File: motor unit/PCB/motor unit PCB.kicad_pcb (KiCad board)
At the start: 2 copper layers, 17.5 x 17.1 mm, 6 parts, among them M1 2RB18Z1B5, P1 CONN, Q1 2N7002

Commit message: Update motor unit PCB files
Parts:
- moved D1 8.71 mm to (161.5, 75.9)
- moved P1 8.13 mm to (159.0, 64.5), turned to 90 degrees
- moved C1 5.06 mm to (168.7, 64.3), turned to 180 degrees
- moved M1 4.26 mm to (168.7, 67.8)
- moved Q1 3.42 mm to (161.5, 72.4)
- moved R1 2.60 mm to (161.5, 68.3)
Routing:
- net Net-(C1-Pad2): track 30.5 -> 17.5 mm
- net +5V: track 14.9 -> 3.77 mm
- net GND: track 4.50 -> 7.86 mm
- net Net-(P1-Pad3): track 9.94 -> 7.86 mm
- added copper zone on F.Cu, net +5V
- removed copper zone on F.Cu, net GND

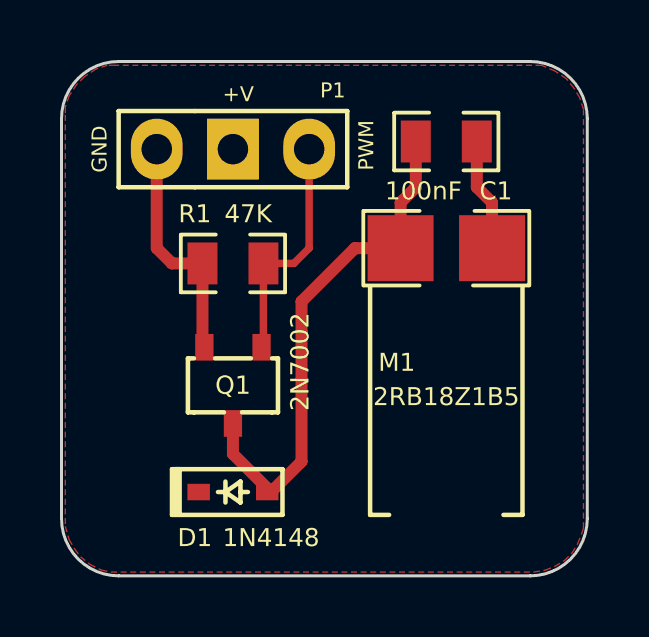
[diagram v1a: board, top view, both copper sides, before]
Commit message: Update motor unit 3D and PCB
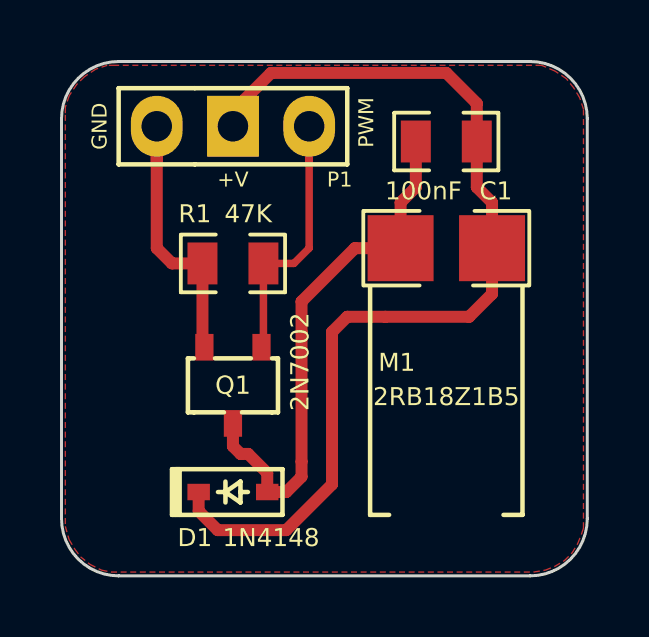
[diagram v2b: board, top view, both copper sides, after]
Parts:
- moved P1 0.76 mm to (159.0, 63.8)
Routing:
- net +5V: track 3.77 -> 33.1 mm
- net Net-(P1-Pad3): track 7.86 -> 9.13 mm
- net GND: track 7.86 -> 9.13 mm
- net Net-(C1-Pad2): track 17.5 -> 18.0 mm
- added copper zone on F.Cu, net GND
- removed copper zone on F.Cu, net +5V
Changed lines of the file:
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@@
     (links 10)
     (no_connects 0)
-    (area 155.778999 61.544999 173.405001 78.790001)
+    (area 153.557572 61.544999 173.405001 78.790001)
     (thickness 1.6)
     (drawings 8)
-    (tracks 25)
+    (tracks 48)
     (zones 0)
     (modules 6)
@@
   )
   (module Pin_Header_Straight_1x03_MOD (layer F.Cu)
-    (at 159.004 64.516 90)
+    (at 159.004 63.754 90)
     (descr "Through hole pin header")
     (tags "pin header")
-    (fp_text reference P1 (at 1.9558 5.8674 180) (layer F.SilkS)
+    (fp_text reference P1 (at -1.778 6.096 180) (layer F.SilkS)
       (effects (font (size 0.5 0.5) (thickness 0.125)))
     )
@@
       (effects (font (size 0.5 0.5) (thickness 0.125)))
     )
-    (fp_text user +V (at 1.8288 2.7178 180) (layer F.SilkS)
+    (fp_text user +V (at -1.778 2.54 180) (layer F.SilkS)
       (effects (font (size 0.5 0.5) (thickness 0.125)))
     )
@@
   (gr_arc (start 157.734 63.5) (end 155.829 63.5) (angle 90) (layer Edge.Cuts) (width 0.1))
   (gr_arc (start 171.45 63.5) (end 171.45 61.595) (angle 90) (layer Edge.Cuts) (width 0.1))
+  (segment (start 162.687 75.946) (end 163.322 75.946) (width 0.4) (layer F.Cu) (net 1))
   (segment (start 163.83 70.612) (end 163.83 69.596) (width 0.4) (layer F.Cu) (net 1))
   (segment (start 163.83 74.93) (end 163.83 70.612) (width 0.4) (layer F.Cu) (net 1))
-  (segment (start 162.814 75.946) (end 163.83 74.93) (width 0.4) (layer F.Cu) (net 1))
   (segment (start 165.608 67.818) (end 167.132 67.818) (width 0.4) (layer F.Cu) (net 1))
   (segment (start 163.83 69.596) (end 165.608 67.818) (width 0.4) (layer F.Cu) (net 1))
+  (segment (start 163.83 75.438) (end 163.83 74.93) (width 0.4) (layer F.Cu) (net 1))
+  (segment (start 163.322 75.946) (end 163.83 75.438) (width 0.4) (layer F.Cu) (net 1))
+  (segment (start 162.687 75.946) (end 162.687 75.311) (width 0.4) (layer F.Cu) (net 1))
+  (segment (start 161.544 74.422) (end 161.544 73.66) (width 0.4) (layer F.Cu) (net 1))
+  (segment (start 161.798 74.676) (end 161.544 74.422) (width 0.4) (layer F.Cu) (net 1))
+  (segment (start 162.052 74.676) (end 161.798 74.676) (width 0.4) (layer F.Cu) (net 1))
+  (segment (start 162.687 75.311) (end 162.052 74.676) (width 0.4) (layer F.Cu) (net 1))
+  (segment (start 162.687 75.946) (end 162.814 75.946) (width 0.4) (layer F.Cu) (net 1))
+  (segment (start 167.132 66.294) (end 167.132 67.818) (width 0.4) (layer F.Cu) (net 1))
   (segment (start 167.64 64.262) (end 167.64 65.786) (width 0.4) (layer F.Cu) (net 1))
   (segment (start 167.64 65.786) (end 167.132 66.294) (width 0.4) (layer F.Cu) (net 1))
-  (segment (start 167.132 66.294) (end 167.132 67.818) (width 0.4) (layer F.Cu) (net 1))
-  (segment (start 162.687 75.946) (end 162.814 75.946) (width 0.4) (layer F.Cu) (net 1))
-  (segment (start 161.544 73.66) (end 161.544 74.676) (width 0.4) (layer F.Cu) (net 1))
-  (segment (start 161.544 74.676) (end 162.687 75.819) (width 0.4) (layer F.Cu) (net 1))
-  (segment (start 162.687 75.819) (end 162.687 75.946) (width 0.4) (layer F.Cu) (net 1))
+  (segment (start 159.004 63.754) (end 159.004 65.024) (width 0.4) (layer F.Cu) (net 2) (status 400000))
+  (segment (start 159.004 67.818) (end 159.512 68.326) (width 0.4) (layer F.Cu) (net 2))
+  (segment (start 159.512 68.326) (end 160.528 68.326) (width 0.4) (layer F.Cu) (net 2))
+  (segment (start 159.004 64.516) (end 159.004 65.024) (width 0.4) (layer F.Cu) (net 2))
+  (segment (start 159.004 65.024) (end 159.004 67.818) (width 0.4) (layer F.Cu) (net 2))
+  (segment (start 160.528 71.0565) (end 160.5915 71.12) (width 0.4) (layer F.Cu) (net 2))
   (segment (start 160.528 68.326) (end 160.528 71.0565) (width 0.4) (layer F.Cu) (net 2))
-  (segment (start 160.528 71.0565) (end 160.5915 71.12) (width 0.4) (layer F.Cu) (net 2))
-  (segment (start 159.004 64.516) (end 159.004 67.818) (width 0.4) (layer F.Cu) (net 2))
-  (segment (start 159.512 68.326) (end 160.528 68.326) (width 0.4) (layer F.Cu) (net 2))
-  (segment (start 159.004 67.818) (end 159.512 68.326) (width 0.4) (layer F.Cu) (net 2))
+  (segment (start 161.544 63.754) (end 161.544 63.246) (width 0.4) (layer F.Cu) (net 3) (status C00000))
+  (segment (start 161.544 63.246) (end 162.814 61.976) (width 0.4) (layer F.Cu) (net 3) (status 400000))
+  (segment (start 162.814 61.976) (end 168.656 61.976) (width 0.4) (layer F.Cu) (net 3))
+  (segment (start 168.656 61.976) (end 169.672 62.992) (width 0.4) (layer F.Cu) (net 3))
+  (segment (start 169.672 62.992) (end 169.672 64.262) (width 0.4) (layer F.Cu) (net 3) (status 800000))
+  (segment (start 166.624 70.104) (end 165.354 70.104) (width 0.4) (layer F.Cu) (net 3))
+  (segment (start 166.624 70.104) (end 169.418 70.104) (width 0.4) (layer F.Cu) (net 3))
+  (segment (start 169.418 70.104) (end 170.18 69.342) (width 0.4) (layer F.Cu) (net 3))
+  (segment (start 170.18 67.818) (end 170.18 69.342) (width 0.4) (layer F.Cu) (net 3))
+  (segment (start 164.846 75.692) (end 163.322 77.216) (width 0.4) (layer F.Cu) (net 3))
+  (segment (start 164.846 70.612) (end 164.846 75.692) (width 0.4) (layer F.Cu) (net 3))
+  (segment (start 165.354 70.104) (end 164.846 70.612) (width 0.4) (layer F.Cu) (net 3))
+  (segment (start 160.401 75.946) (end 160.401 76.581) (width 0.4) (layer F.Cu) (net 3))
+  (segment (start 160.401 76.581) (end 161.036 77.216) (width 0.4) (layer F.Cu) (net 3))
+  (segment (start 161.036 77.216) (end 163.322 77.216) (width 0.4) (layer F.Cu) (net 3))
+  (segment (start 169.672 65.786) (end 170.18 66.294) (width 0.4) (layer F.Cu) (net 3))
+  (segment (start 170.18 66.294) (end 170.18 67.818) (width 0.4) (layer F.Cu) (net 3))
   (segment (start 169.672 64.262) (end 169.672 65.786) (width 0.4) (layer F.Cu) (net 3))
-  (segment (start 170.18 66.294) (end 170.18 67.818) (width 0.4) (layer F.Cu) (net 3))
-  (segment (start 169.672 65.786) (end 170.18 66.294) (width 0.4) (layer F.Cu) (net 3))
+  (segment (start 164.084 63.754) (end 164.084 65.024) (width 0.25) (layer F.Cu) (net 4) (status 400000))
+  (segment (start 164.084 67.818) (end 163.576 68.326) (width 0.25) (layer F.Cu) (net 4))
+  (segment (start 163.576 68.326) (end 162.56 68.326) (width 0.25) (layer F.Cu) (net 4))
+  (segment (start 164.084 64.516) (end 164.084 65.024) (width 0.25) (layer F.Cu) (net 4))
+  (segment (start 164.084 65.024) (end 164.084 67.818) (width 0.25) (layer F.Cu) (net 4))
+  (segment (start 162.56 71.0565) (end 162.4965 71.12) (width 0.25) (layer F.Cu) (net 4))
   (segment (start 162.56 68.326) (end 162.56 71.0565) (width 0.25) (layer F.Cu) (net 4))
-  (segment (start 162.56 71.0565) (end 162.4965 71.12) (width 0.25) (layer F.Cu) (net 4))
-  (segment (start 164.084 64.516) (end 164.084 67.818) (width 0.25) (layer F.Cu) (net 4))
-  (segment (start 163.576 68.326) (end 162.56 68.326) (width 0.25) (layer F.Cu) (net 4))
-  (segment (start 164.084 67.818) (end 163.576 68.326) (width 0.25) (layer F.Cu) (net 4))
-  (zone (net 3) (net_name +5V) (layer F.Cu) (hatch edge 0.508)
+  (zone (net 2) (net_name GND) (layer F.Cu) (hatch edge 0.508)
     (connect_pads (clearance 0.508))
     (min_thickness 0.254)
